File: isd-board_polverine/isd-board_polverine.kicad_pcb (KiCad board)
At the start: 2 copper layers, 90 x 50 mm, 27 parts, among them J1 BATT, J10 Conn_01x02_Pin, J12 Conn_02x10_Odd_Even, J3 Conn_01x02_Pin, J4 Conn_02x08_Odd_Even, J5 Conn_02x08_Odd_Even, J8 USB_C_Receptacle_PowerOnly_6P, J9 Conn_01x04_Socket, Q1 Q_Dual_NMOS_S1G1D2S2G2D1, U1 DW01A

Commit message: update: battery protection circuit (compact placement)
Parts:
- Q1: value Q_Dual_NMOS_S1G1D2S2G2D1 -> DMG9926UDM; footprint Package_TO_SOT_SMD:SOT-23-6_Handsoldering -> Package_TO_SOT_SMD:SOT-23-6
- moved C1 11.4 mm to (110.3, 55.2), turned to 180 degrees
- moved C2 11.0 mm to (116.0, 53.4), turned to -90 degrees
- moved F1 9.03 mm to (106.4, 50.7)
- moved TP6 6.76 mm to (116.0, 48.9), turned to 0 degrees
- moved Q1 6.35 mm to (105.6, 59.5), turned to -90 degrees
- moved U1 5.97 mm to (110.6, 59.7), turned to 90 degrees
- moved R1 3.62 mm to (113.6, 53.4)
- moved R2 3.22 mm to (109.5, 63.8)
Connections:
- Q1 pad 2: Net-(Q1A-G) -> Net-(Q1-S1/D2-Pad2)
- Q1 pad 3: Net-(Q1A-D) -> GND
- Q1 pad 4: GND -> Net-(Q1-G2)
- Q1 pad 5: Net-(Q1B-G) -> Net-(Q1-S1/D2-Pad2)
- Q1 pad 6: Net-(Q1A-D) -> Net-(Q1-G1)
- U1 pad 1: Net-(Q1A-G) -> Net-(Q1-G1)
- U1 pad 3: Net-(Q1B-G) -> Net-(Q1-G2)
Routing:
- net +BATT: track 27.6 -> 11.9 mm
- net Net-(Q1A-G): track 12.1 -> 0.00 mm
- net Net-(U1-VCC): track 17.0 -> 6.07 mm
- net Net-(Q1-G2): track 0.00 -> 10.4 mm, vias 0 -> 2
- net Net-(Q1B-G): track 10.2 -> 0.00 mm
- net Net-(J1-Pin_2): track 28.2 -> 18.2 mm
- net Net-(J1-Pin_1): track 16.4 -> 6.67 mm
- net Net-(Q1A-D): track 4.31 -> 0.00 mm
- net Net-(Q1-G1): track 0.00 -> 3.27 mm
- net Net-(Q1-S1/D2-Pad2): track 0.00 -> 2.28 mm
- net Net-(U1-CS): track 3.32 -> 2.79 mm
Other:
- board text removed: "BAT"
- board text removed: "SOLAR"

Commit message: update: dual-socket sch/pcb (polverine socket, dfr1117 socket, grove-conn, zif-conn (bmv080), lga 3x3mm (bme690), b5b-zr (sps30))
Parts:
- added C3: 1µF, Capacitor_SMD:C_0805_2012Metric_Pad1.18x1.45mm_HandSolder, F.Cu at (125.5, 89.5)
- added J11: Conn_01x08, Package_LGA:Bosch_LGA-8_3x3mm_P0.8mm_ClockwisePinNumbering, F.Cu at (136.3, 82.9)
- added J2: Conn_01x04_Socket, Connector:NS-Tech_Grove_1x04_P2mm_Vertical, F.Cu at (141.2, 66.6)
- added J6: Conn_01x05_Socket, Connector_JST:JST_ZH_B5B-ZR_1x05_P1.50mm_Vertical, F.Cu at (143.2, 51.9)
- added J7: Conn_01x08, Connector_PinSocket_2.54mm:PinSocket_1x08_P2.54mm_Vertical, F.Cu at (175.3, 69.7)
- J10: value Conn_01x02_Pin -> Conn_01x08; footprint Connector_PinHeader_2.54mm:PinHeader_1x02_P2.54mm_Vertical -> Connector_PinSocket_2.54mm:PinSocket_1x08_P2.54mm_Vertical
- J12: value Conn_02x10_Odd_Even -> 5035661302; footprint Connector_PinHeader_2.54mm:PinHeader_2x10_P2.54mm_Vertical -> footprint:CON_5035661302_MOL
- moved J9 40.7 mm to (161.6, 87.9), turned to 90 degrees
- moved J10 37.6 mm to (175.3, 51.9), turned to -90 degrees
- moved J12 24.6 mm to (125.3, 84.8)
- moved R16 9.36 mm to (132.2, 47.8)
- moved R15 9.36 mm to (124.2, 47.8)
- moved C14 9.36 mm to (128.3, 47.8)
- moved J5 8.01 mm to (157.6, 63.5)
- moved J4 3.59 mm to (157.5, 78.7)
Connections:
- J10 pad 1: /RST -> GND
- J10 pad 2: GND -> +3V3
- J12 pad 1: /TMS -> +3V3
- J12 pad 10: GND -> +3V3
- J12 pad 11: /SCL -> GND
- J12 pad 12: /PWM -> /BMV080_IRQ
- J12 pad 13: /SDA -> unconnected-(J12-Pad13)
- J12 pad 2: /CS -> GND
- J12 pad 3: /TDI -> +3V3
- J12 pad 4: /SCK -> GND
- J12 pad 5: /TDO -> /BME690_SDA
- J12 pad 6: /MISO -> /BME690_SCL
- J12 pad 7: /TCK -> /BMV080_PS
- J12 pad 8: /MOSI -> +3V3
- J3 pad 1: unconnected-(J3-Pin_1-Pad1) -> /V_SOLAR
- J3 pad 2: unconnected-(J3-Pin_2-Pad2) -> GND
- J4 pad 14: +3V3 -> unconnected-(J4-Pin_14-Pad14)
- J4 pad 15: unconnected-(J4-Pin_15-Pad15) -> +3V3
- J5 pad 10: unconnected-(J5-Pin_10-Pad10) -> +5V
- J5 pad 11: /SDA -> /BME690_SDA
- J5 pad 13: unconnected-(J5-Pin_13-Pad13) -> +5V
- J5 pad 9: /SCL -> /BME690_SCL
- J9 pad 1: /TX -> /RX
- J9 pad 2: /RX -> /TX
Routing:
- net /BME690_SDA: track 0.00 -> 103.5 mm, vias 0 -> 3
- net /BME690_SCL: track 0.00 -> 100.2 mm, vias 0 -> 4
- net +5V: track 0.00 -> 72.8 mm, vias 0 -> 3
- net /AN: track 48.7 -> 1.74 mm, vias 2 -> 1
- net +3V3: track 74.7 -> 108.6 mm, vias 1 -> 4
- net /SDA: track 33.1 -> 0.00 mm, vias 1 -> 0
- net /SCL: track 33.0 -> 0.00 mm, vias 1 -> 0
- net /PWM: track 31.5 -> 0.00 mm
- net /INT: track 31.2 -> 0.00 mm
- net /TXD0: track 29.9 -> 0.00 mm, vias 1 -> 0
- net /TCK: track 29.3 -> 0.00 mm
- net /CS: track 29.1 -> 0.00 mm
- net /RXD0: track 29.0 -> 0.00 mm, vias 1 -> 0
- net /TDO: track 28.7 -> 0.00 mm
- net /TDI: track 26.7 -> 0.00 mm
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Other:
- board text added: "5V"
- board text added: "BMV080"
- board text added: "BOSCH"
- board text added: "BOSCH BME690"
- board text added: "I2C"
- board text added: "ISD-BOARD DUAL SOCKET v0.1"
- board text added: "POLVERINE & DFR1117 ANT. ZONE"
- board text added: "RX"
- board text added: "TX"
- board text added: "[DFR1117 SLOT]"
- board text added: "[POLVERINE SLOT]"
- board text removed: "-"
- board text removed: "CS"
- board text removed: "INT"
- board text removed: "ISD-BOARD Polverine + MPTT v0.1"
- board text removed: "MISO"
- board text removed: "MOSI"
- board text removed: "PWM"
- board text removed: "RST / GND"
- board text removed: "RX / TX"
- board text removed: "RXD0"
- board text removed: "SCK"
- board text removed: "STAT"
- board text removed: "TCK"
- board text removed: "TDI"
- board text removed: "TDO"
- board text removed: "TMS"
- board text removed: "TXD0"
- board text removed: "USB"

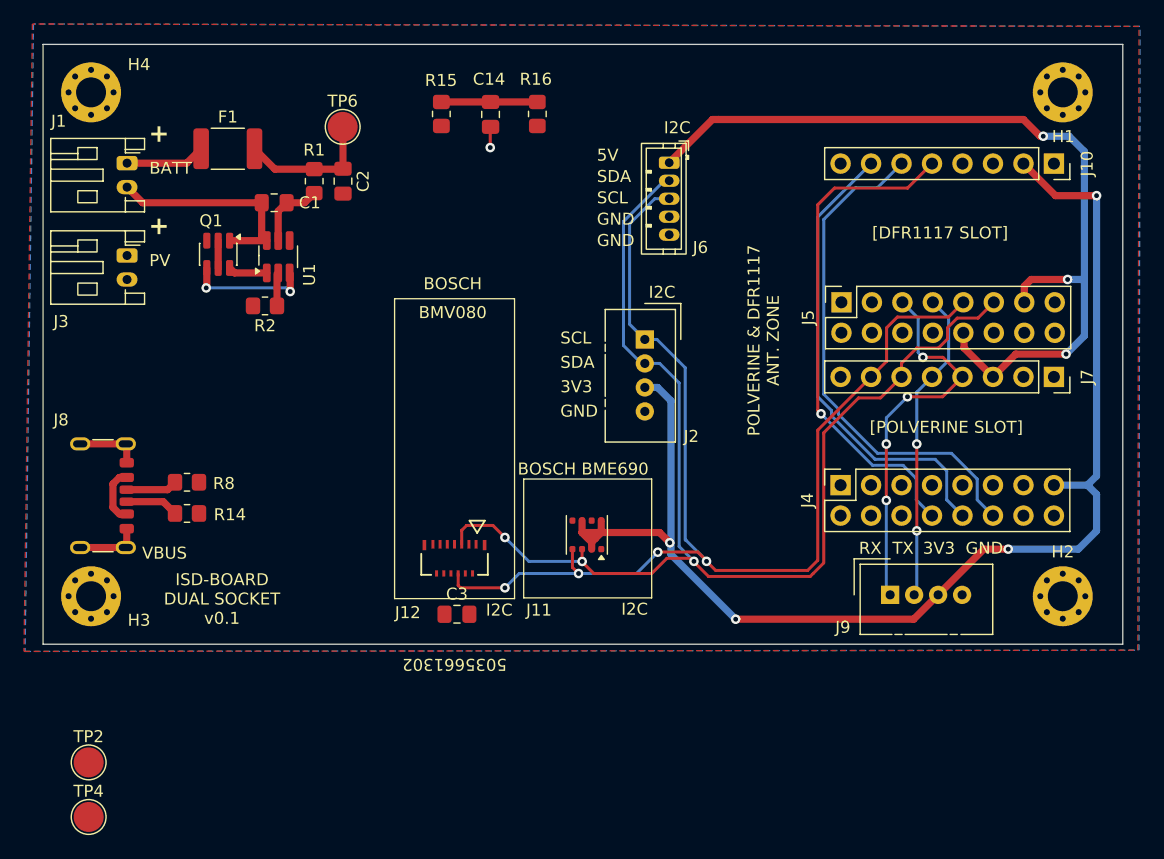
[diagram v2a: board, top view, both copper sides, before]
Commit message: update: sch/pcb (pin routing, bmv690/bmv080 footprints, power switch ic)
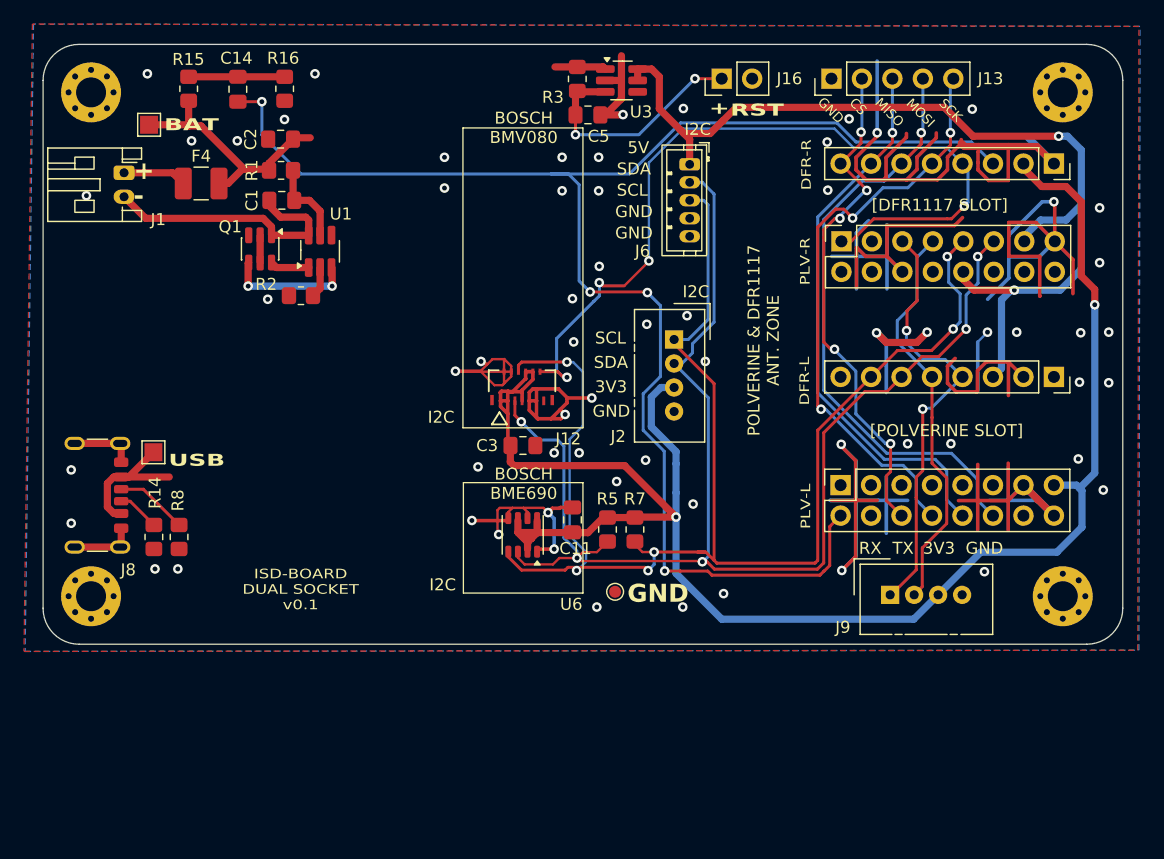
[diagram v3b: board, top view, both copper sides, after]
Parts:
- removed F1: MINIASMDC075F, Fuse:Fuse_1812_4532Metric_Pad1.30x3.40mm_HandSolder
- removed J11: Conn_01x08, Package_LGA:Bosch_LGA-8_3x3mm_P0.8mm_ClockwisePinNumbering
- removed J3: Conn_01x02_Pin, Connector_JST:JST_PH_S2B-PH-K_1x02_P2.00mm_Horizontal
- removed TP2: TP_VBUS, TestPoint:TestPoint_Pad_D2.5mm
- added C11: 10µF, Capacitor_SMD:C_0805_2012Metric_Pad1.18x1.45mm_HandSolder, F.Cu at (135.1, 81.6)
- added C5: 0.1µF, Capacitor_SMD:C_0805_2012Metric_Pad1.18x1.45mm_HandSolder, F.Cu at (136.4, 47.9)
- added F4: 1.1A, 12V, Fuse:Fuse_1210_3225Metric_Pad1.42x2.65mm_HandSolder, F.Cu at (104.2, 53.6)
- added J13: Conn_01x05, Connector_PinHeader_2.54mm:PinHeader_1x05_P2.54mm_Vertical, F.Cu at (156.7, 44.9)
- added J16: Conn_01x02, Connector_PinHeader_2.54mm:PinHeader_1x02_P2.54mm_Vertical, F.Cu at (147.6, 44.9)
- added R3: 10k, Resistor_SMD:R_0805_2012Metric_Pad1.20x1.40mm_HandSolder, F.Cu at (135.5, 44.9)
- added R5: 10k, Resistor_SMD:R_0805_2012Metric_Pad1.20x1.40mm_HandSolder, F.Cu at (138.0, 82.4)
- added R7: 10k, Resistor_SMD:R_0805_2012Metric_Pad1.20x1.40mm_HandSolder, F.Cu at (140.3, 82.4)
- added TP1: TP_VBUS, TestPoint:TestPoint_Pad_1.5x1.5mm, F.Cu at (100.2, 76.0)
- added U3: TPS22917DBV, Package_TO_SOT_SMD:SOT-23-6_Handsoldering, F.Cu at (139.2, 45.0)
- added U6: BME680, Package_LGA:Bosch_LGA-8_3x3mm_P0.8mm_ClockwisePinNumbering, F.Cu at (131.0, 82.9)
- C3: value 1µF -> 10µF
- J1: value BATT -> Conn_01x02_Socket
- Q1: value DMG9926UDM -> Dual NMos
- TP4: footprint TestPoint:TestPoint_Pad_D2.5mm -> TestPoint:TestPoint_Pad_D1.0mm
- TP6: footprint TestPoint:TestPoint_Pad_D2.5mm -> TestPoint:TestPoint_Pad_1.5x1.5mm
- moved TP4 47.7 mm to (138.7, 87.6)
- moved C14 21.2 mm to (107.2, 45.7)
- moved R15 21.2 mm to (103.1, 45.7)
- moved R16 21.2 mm to (111.1, 45.7)
- moved TP6 16.1 mm to (99.8, 48.7)
- moved J12 15.3 mm to (130.9, 70.6), turned to 0 degrees
- moved C3 15.1 mm to (131.0, 75.4)
- moved C2 6.27 mm to (110.8, 49.9), turned to 180 degrees
- moved J5 5.08 mm to (157.6, 58.4)
- moved R8 4.61 mm to (102.3, 83.1), turned to -90 degrees
- moved Q1 3.52 mm to (109.1, 59.0)
- moved U1 3.52 mm to (114.1, 59.2)
- moved R14 3.39 mm to (100.2, 83.1), turned to -90 degrees
- moved R2 3.11 mm to (112.5, 63.0)
- moved R1 2.91 mm to (110.8, 52.5), turned to 180 degrees
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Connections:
- net Net-(J1-Pin_2) renamed -BATT
- C14 pad 2: /AN -> /ADC_BATT
- J10 pad 3: /LP_RX -> /ADC_BATT
- J10 pad 4: /LP_TX -> /BMV080_IRQ
- J10 pad 8: /LP_SCL -> /CS
- J12 pad 7: /BMV080_PS -> +3V3
- J4 pad 2: /AN -> /ADC_BATT
- J5 pad 1: /PWM -> /BMV080_IRQ
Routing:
- net GND: track 11.1 -> 302.8 mm, vias 0 -> 65
- net /ADC_BATT: track 0.00 -> 130.9 mm, vias 0 -> 4
- net /BMV080_IRQ: track 0.00 -> 69.7 mm, vias 0 -> 4
- net /CS: track 0.00 -> 43.3 mm, vias 0 -> 5
- net +3V3: track 108.6 -> 145.2 mm, vias 4 -> 2
- net /BME690_SCL: track 100.2 -> 124.8 mm, vias 4 -> 6
- net Net-(J16-Pin_1): track 0.00 -> 20.2 mm, vias 0 -> 2
- net /BME690_SDA: track 103.5 -> 118.5 mm, vias 3 -> 5
- net +5V: track 72.8 -> 83.9 mm, vias 3 -> 2
- net +BATT: track 11.9 -> 21.3 mm
- net /TX: track 26.1 -> 33.9 mm, vias 2 -> 0
- net /SCK: track 42.3 -> 50.0 mm, vias 1 -> 3
- net VBUS: track 4.71 -> 12.3 mm
- net /MISO: track 39.1 -> 46.4 mm, vias 0 -> 1
- net /MOSI: track 42.6 -> 49.9 mm, vias 0 -> 1
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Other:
- outline, holes or cut-outs redrawn
- board text added: "-"
- board text added: "BAT"
- board text added: "BOSCH BMV080"
- board text added: "CS"
- board text added: "DFR-L"
- board text added: "DFR-R"
- board text added: "MISO"
- board text added: "MOSI"
- board text added: "PLV-L"
- board text added: "PLV-R"
- board text added: "RST"
- board text added: "SCK"
- board text added: "USB"
- board text removed: "BATT"
- board text removed: "BMV080"
- board text removed: "BOSCH"
- board text removed: "PV"
- board text removed: "VBUS"
